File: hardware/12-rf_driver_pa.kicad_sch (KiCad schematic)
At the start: 33 parts, among them J11 Conn_Coaxial, U2 GRF5115, U3 GRF5115

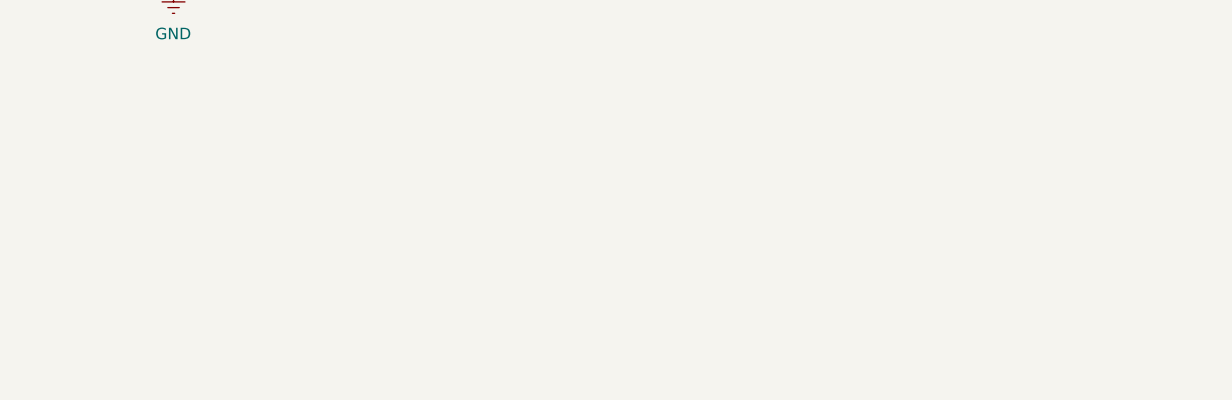
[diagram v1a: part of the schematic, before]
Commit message: Updated sheet names, added s-band initial block diagram
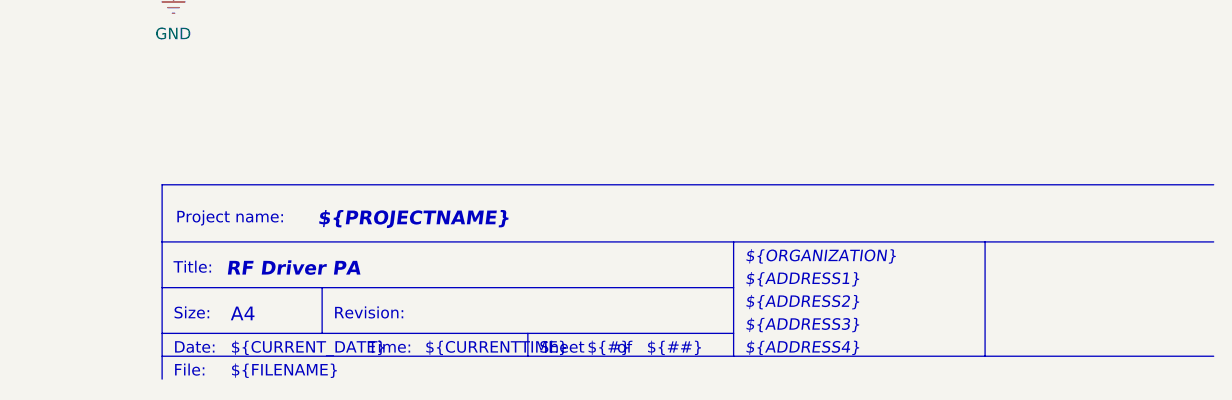
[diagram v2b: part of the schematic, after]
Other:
- note added: "${##}"
- note added: "${#}"
- note added: "${ADDRESS1}"
- note added: "${ADDRESS2}"
- note added: "${ADDRESS3}"
- note added: "${ADDRESS4}"
- note added: "${CURRENTTIME}"
- note added: "${CURRENT_DATE}"
- note added: "${FILENAME}"
- note added: "${ORGANIZATION}"
- note added: "${PROJECTNAME}"
- note added: "${REVISION}"
- note added: "${TITLE}"
- note added: "A4"
- note added: "Date:"
- note added: "File:"
- note added: "Project name:"
- note added: "Revision:"
- note added: "Sheet"
- note added: "Size:"
- note added: "Time:"
- note added: "Title:"
- note added: "of"
- title: (none) -> RF Driver PA

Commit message: Added RF Tools plugin for KiCAD v10, rerouted FPGA JTAG and FPGA EGPIO connectors and tracks, rerouted VCC5P0 track, added via fence around RF tracks.
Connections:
- net GND: now also U2.5 (GND/NC), U2.6 (GND/NC), U2.7 (GND/NC), U2.8 (GND/NC), U3.5 (GND/NC), U3.6 (GND/NC), U3.7 (GND/NC), U3.8 (GND/NC)
